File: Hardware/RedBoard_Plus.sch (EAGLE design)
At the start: 80 parts, among them IC3 LM1117, J2 ISP, J3 5.5x2.1mm Barrel, J4 QWIIC_RIGHT_ANGLE, J5 USB Female Type C Connector, Q1 20V/4.2A/52mΩ/1.4W, Q2 310mA/60V/1.6Ω, Q3 310mA/60V/1.6Ω, U3 3.3V, U4 ATMEGA328P_TQFP, U5 CH340C, Y1 16MHz

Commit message: Pete's design review notes:
SF logo on back
GND vias next to USB C
Remove 4-way nodes on sch
Remove overlapping text on sch
Move SFE logo in sch
Sch typo
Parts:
- removed U$78: REDBOARD_LOGO, redboard_logo:REDBOARD_LOGO
- added U$3: REDBOARD_LOGO, redboard_logo:REDBOARD_LOGO
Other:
- note added: "This switch is limited to 1.2A."
- note removed: "This switch is limited to 1.2VA."
- moved on the sheet: C8
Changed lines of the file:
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@@
 <attribute name="PROD_ID" value="DIO-09911"/>
 </part>
-<part name="SUPPLY7" library="SparkFun-PowerSymbols" deviceset="VIN" device=""/>
 <part name="D1" library="SparkFun-DiscreteSemi" deviceset="DIODE-SCHOTTKY" device="-SS14" value="1A/40V/500mV"/>
 <part name="JP11" library="SparkFun-Connectors" deviceset="M08" device="SMD-COMBO" value="JP11">
@@
 <part name="GND9" library="SparkFun-PowerSymbols" deviceset="GND" device=""/>
 <part name="J1" library="SparkFun-Connectors" deviceset="CONN_02" device="1X02_NO_SILK"/>
-<part name="U$78" library="redboard_logo" deviceset="REDBOARD_LOGO" device=""/>
-<part name="U$1" library="redboard_logo" deviceset="REDBOARD_LOGO" device=""/>
 <part name="FD1" library="SparkFun-Aesthetics" deviceset="FIDUCIAL" device="1X2"/>
 <part name="FD2" library="SparkFun-Aesthetics" deviceset="FIDUCIAL" device="1X2"/>
+<part name="U$1" library="redboard_logo" deviceset="REDBOARD_LOGO" device=""/>
+<part name="U$3" library="redboard_logo" deviceset="REDBOARD_LOGO" device=""/>
+<part name="SUPPLY25" library="SparkFun-PowerSymbols" deviceset="VIN" device=""/>
 </parts>
 <sheets>
@@
 30.8 mil width
 https://www.eeweb.com/tools/external-pcb-trace-max-current</text>
-<text x="220.98" y="144.78" size="1.778" layer="97" font="vector">This switch is limited to 1.2VA.</text>
+<text x="220.98" y="144.78" size="1.778" layer="97" font="vector">This switch is limited to 1.2A.</text>
 <wire x1="215.9" y1="279.4" x2="215.9" y2="81.28" width="0.2032" layer="97" style="longdash"/>
 <text x="183.642" y="264.16" size="2.54" layer="97" font="vector" align="center">PTH Connections</text>
@@
 <attribute name="VALUE" x="264.16" y="195.834" size="1.778" layer="96" align="bottom-center"/>
 </instance>
-<instance part="C8" gate="G$1" x="38.1" y="218.44" smashed="yes" rot="R90">
-<attribute name="NAME" x="35.179" y="219.964" size="1.778" layer="95" font="vector" rot="R90"/>
-<attribute name="VALUE" x="40.259" y="219.964" size="1.778" layer="96" font="vector" rot="R90"/>
+<instance part="C8" gate="G$1" x="35.56" y="218.44" smashed="yes" rot="R90">
+<attribute name="NAME" x="32.639" y="219.964" size="1.778" layer="95" font="vector" rot="R90"/>
+<attribute name="VALUE" x="37.719" y="219.964" size="1.778" layer="96" font="vector" rot="R90"/>
 </instance>
 <instance part="C10" gate="G$1" x="45.72" y="17.78" smashed="yes" rot="MR0">
@@
 <attribute name="VALUE" x="60.452" y="194.31" size="1.778" layer="96" font="vector"/>
 </instance>
-<instance part="JP1" gate="G$1" x="55.88" y="231.14" smashed="yes"/>
-<instance part="JP7" gate="G$1" x="83.566" y="242.062" smashed="yes"/>
+<instance part="JP1" gate="G$1" x="243.84" y="2.54" smashed="yes"/>
+<instance part="JP7" gate="G$1" x="233.426" y="5.842" smashed="yes"/>
 <instance part="J2" gate="G$1" x="27.94" y="157.48" smashed="yes">
 <attribute name="NAME" x="22.86" y="163.068" size="1.778" layer="95" font="vector"/>
@@
 <attribute name="VALUE" x="91.948" y="150.495" size="1.778" layer="96" font="vector" align="top-left"/>
 </instance>
-<instance part="SUPPLY7" gate="G$1" x="261.62" y="243.84" smashed="yes">
-<attribute name="VALUE" x="261.62" y="246.634" size="1.778" layer="96" align="bottom-center"/>
-</instance>
 <instance part="D1" gate="G$1" x="243.84" y="241.3" smashed="yes">
 <attribute name="NAME" x="246.38" y="241.7826" size="1.778" layer="95"/>
@@
 <instance part="BYP" gate="G$1" x="53.34" y="45.72" smashed="yes">
 <attribute name="NAME" x="51.054" y="47.752" size="1.778" layer="95" font="vector"/>
-<attribute name="VALUE" x="50.8" y="43.18" size="1.778" layer="96" font="vector" align="top-left"/>
 </instance>
 <instance part="F2" gate="F1" x="53.34" y="33.02" smashed="yes">
@@
 <attribute name="NAME" x="172.72" y="205.232" size="1.778" layer="95" font="vector" rot="R180"/>
 </instance>
-<instance part="U$78" gate="G$1" x="403.86" y="40.64" smashed="yes"/>
-<instance part="U$1" gate="G$1" x="375.92" y="40.64" smashed="yes"/>
 <instance part="FD1" gate="G$1" x="424.18" y="17.78" smashed="yes"/>
 <instance part="FD2" gate="G$1" x="426.72" y="17.78" smashed="yes"/>
+<instance part="U$1" gate="G$1" x="403.86" y="40.64" smashed="yes"/>
+<instance part="U$3" gate="G$1" x="378.46" y="40.64" smashed="yes"/>
+<instance part="SUPPLY25" gate="G$1" x="259.08" y="243.84" smashed="yes">
+<attribute name="VALUE" x="259.08" y="246.634" size="1.778" layer="96" align="bottom-center"/>
+</instance>
 </instances>
 <busses>
@@
 <pinref part="C5" gate="G$1" pin="+"/>
 <pinref part="IC3" gate="G$1" pin="IN"/>
-<wire x1="261.62" y1="241.3" x2="246.38" y2="241.3" width="0.1524" layer="91"/>
-<pinref part="SUPPLY7" gate="G$1" pin="VIN"/>
+<wire x1="261.62" y1="241.3" x2="259.08" y2="241.3" width="0.1524" layer="91"/>
 <pinref part="D1" gate="G$1" pin="C"/>
-<wire x1="261.62" y1="243.84" x2="261.62" y2="241.3" width="0.1524" layer="91"/>
+<wire x1="259.08" y1="241.3" x2="246.38" y2="241.3" width="0.1524" layer="91"/>
+<wire x1="259.08" y1="241.3" x2="259.08" y2="243.84" width="0.1524" layer="91"/>
+<junction x="259.08" y="241.3"/>
+<pinref part="SUPPLY25" gate="G$1" pin="VIN"/>
 </segment>
 <segment>
@@
 <pinref part="C15" gate="G$1" pin="+"/>
 <wire x1="60.96" y1="33.02" x2="63.5" y2="33.02" width="0.1524" layer="91"/>
-<wire x1="63.5" y1="33.02" x2="68.58" y2="33.02" width="0.1524" layer="91"/>
+<wire x1="63.5" y1="33.02" x2="66.04" y2="33.02" width="0.1524" layer="91"/>
+<wire x1="66.04" y1="33.02" x2="68.58" y2="33.02" width="0.1524" layer="91"/>
 <wire x1="68.58" y1="22.86" x2="68.58" y2="33.02" width="0.1524" layer="91"/>
 <pinref part="C12" gate="G$1" pin="1"/>
@@
 <junction x="68.58" y="33.02"/>
 <pinref part="BYP" gate="G$1" pin="2"/>
-<wire x1="58.42" y1="45.72" x2="63.5" y2="45.72" width="0.1524" layer="91"/>
-<wire x1="63.5" y1="45.72" x2="63.5" y2="33.02" width="0.1524" layer="91"/>
+<wire x1="58.42" y1="45.72" x2="66.04" y2="45.72" width="0.1524" layer="91"/>
 <pinref part="F2" gate="F1" pin="2"/>
+<wire x1="66.04" y1="45.72" x2="66.04" y2="33.02" width="0.1524" layer="91"/>
+<junction x="66.04" y="33.02"/>
 </segment>
 </net>
@@
 <junction x="45.72" y="33.02"/>
 <pinref part="JP14" gate="JP1" pin="1"/>
-<wire x1="35.56" y1="33.02" x2="45.72" y2="33.02" width="0.1524" layer="91"/>
+<wire x1="35.56" y1="33.02" x2="43.18" y2="33.02" width="0.1524" layer="91"/>
+<wire x1="43.18" y1="33.02" x2="45.72" y2="33.02" width="0.1524" layer="91"/>
 <wire x1="25.4" y1="50.8" x2="35.56" y2="50.8" width="0.1524" layer="91"/>
 <wire x1="35.56" y1="50.8" x2="35.56" y2="33.02" width="0.1524" layer="91"/>
 <junction x="35.56" y="33.02"/>
 <pinref part="BYP" gate="G$1" pin="1"/>
-<wire x1="48.26" y1="45.72" x2="45.72" y2="45.72" width="0.1524" layer="91"/>
-<wire x1="45.72" y1="45.72" x2="45.72" y2="33.02" width="0.1524" layer="91"/>
 <pinref part="F2" gate="F1" pin="1"/>
+<wire x1="48.26" y1="45.72" x2="43.18" y2="45.72" width="0.1524" layer="91"/>
+<wire x1="43.18" y1="45.72" x2="43.18" y2="33.02" width="0.1524" layer="91"/>
+<junction x="43.18" y="33.02"/>
 </segment>
 </net>
@@
 <net name="!DTR" class="0">
 <segment>
-<wire x1="33.02" y1="218.44" x2="30.48" y2="218.44" width="0.1524" layer="91"/>
+<wire x1="30.48" y1="218.44" x2="27.94" y2="218.44" width="0.1524" layer="91"/>
 <pinref part="C8" gate="G$1" pin="1"/>
-<label x="30.48" y="218.44" size="1.27" layer="95" font="vector" rot="R180" xref="yes"/>
+<label x="27.94" y="218.44" size="1.27" layer="95" font="vector" rot="R180" xref="yes"/>
 </segment>
 <segment>
@@
 <pinref part="R3" gate="G$1" pin="1"/>
 <pinref part="C8" gate="G$1" pin="2"/>
+<wire x1="38.1" y1="218.44" x2="40.64" y2="218.44" width="0.1524" layer="91"/>
 <wire x1="40.64" y1="218.44" x2="43.18" y2="218.44" width="0.1524" layer="91"/>
-<label x="43.18" y="220.98" size="1.27" layer="95" font="vector" rot="R90" xref="yes"/>
-<wire x1="43.18" y1="220.98" x2="43.18" y2="218.44" width="0.1524" layer="91"/>
 <pinref part="U4" gate="U1" pin="PC6(/RESET)"/>
 <pinref part="S1" gate="G$1" pin="2"/>
-</segment>
-<segment>
+<wire x1="40.64" y1="218.44" x2="40.64" y2="220.98" width="0.1524" layer="91"/>
+<junction x="40.64" y="218.44"/>
+<label x="40.64" y="220.98" size="1.27" layer="95" rot="R90" xref="yes"/>
+</segment>
+<segment>

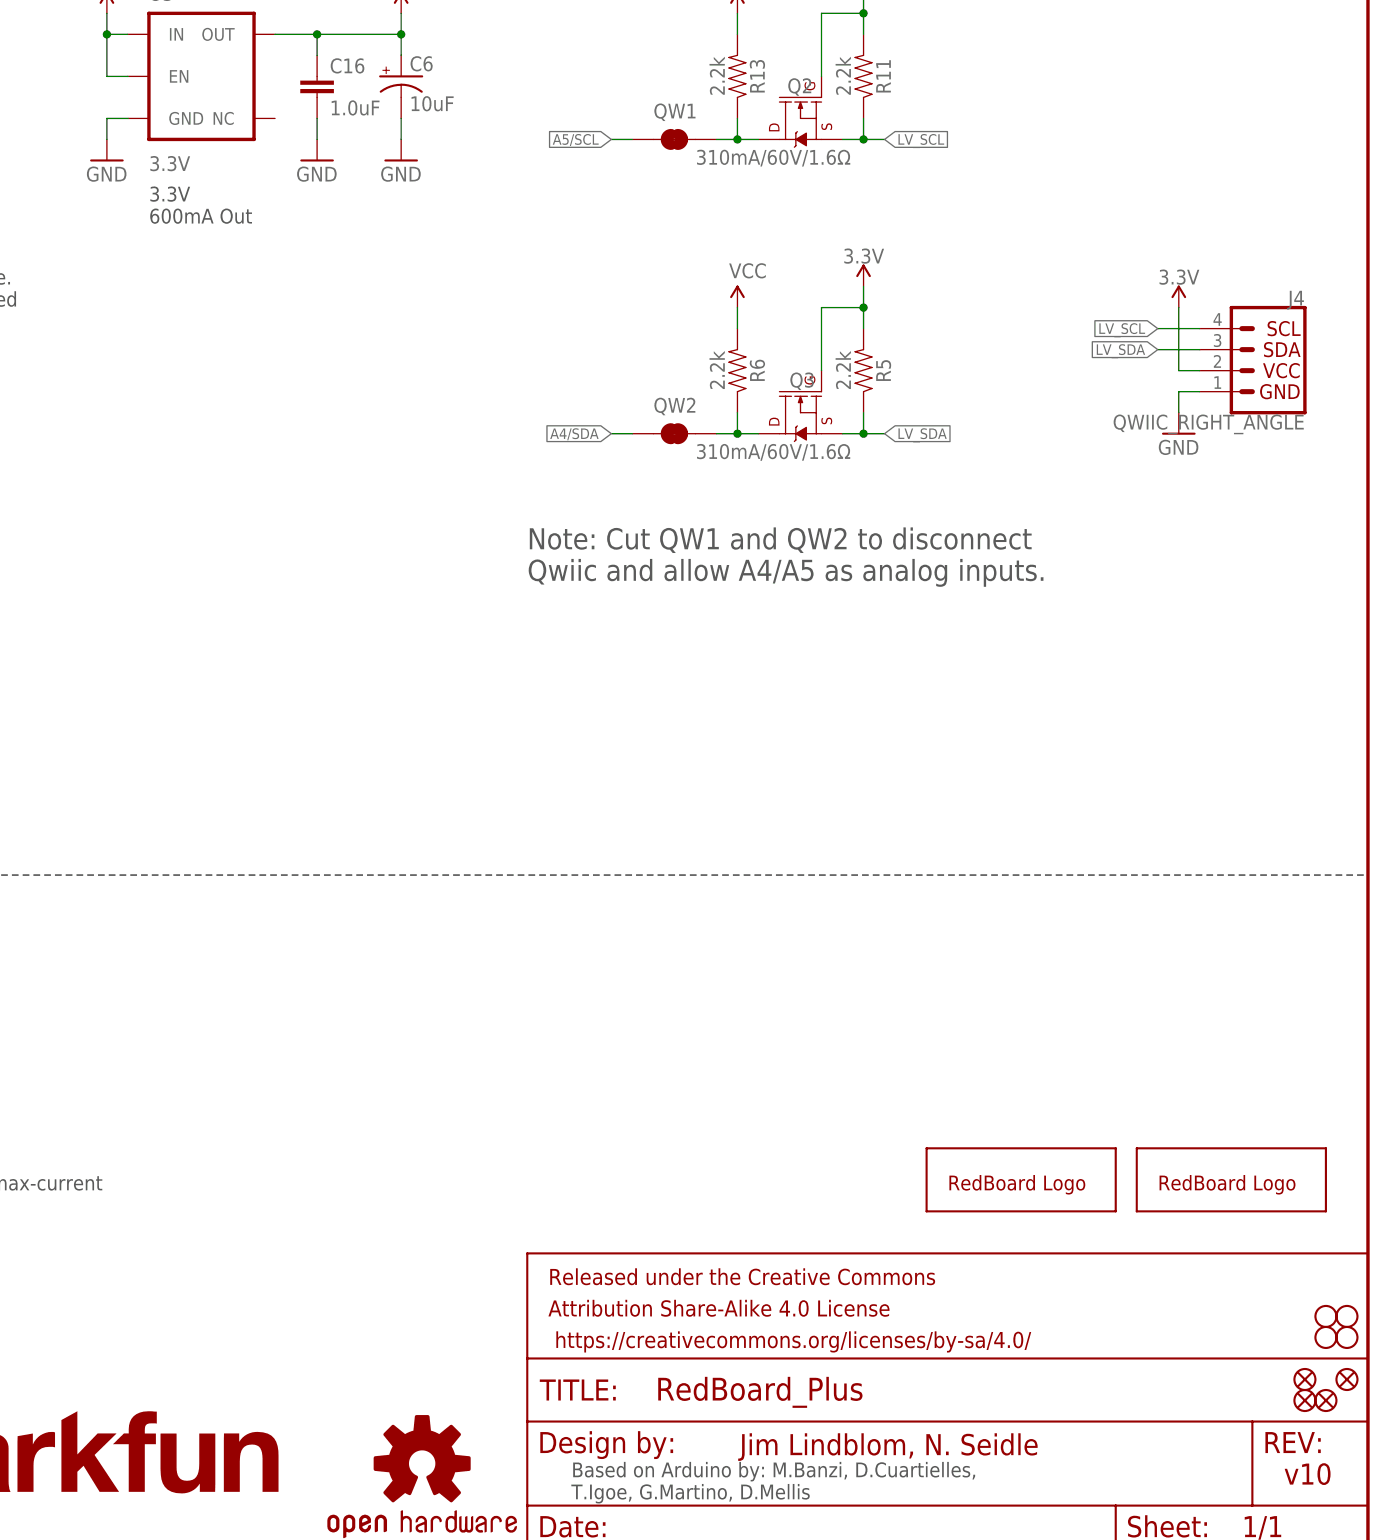
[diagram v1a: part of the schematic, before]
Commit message: Design review changes
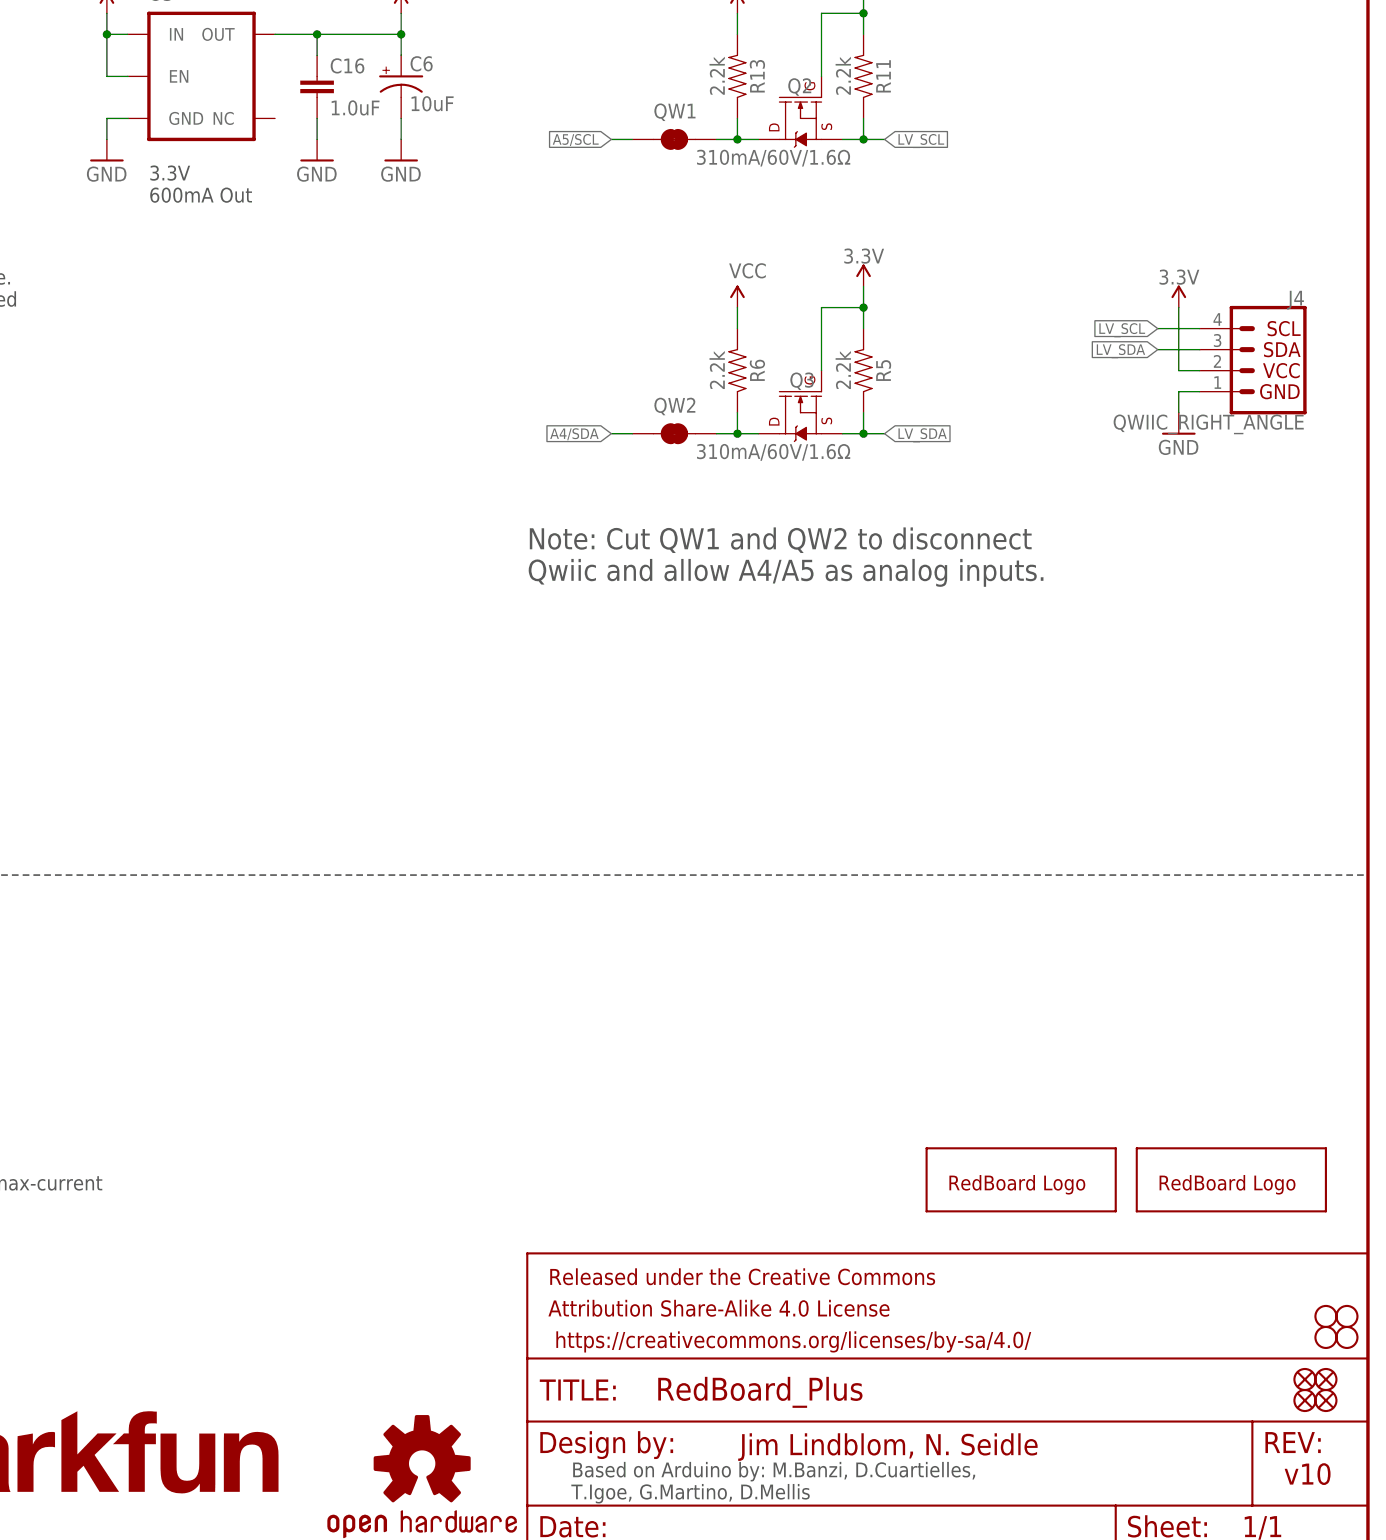
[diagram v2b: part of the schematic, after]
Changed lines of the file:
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@@
 <text x="421.64" y="7.62" size="2.54" layer="94" font="vector">v10</text>
 <text x="225.044" y="245.872" size="1.778" layer="97" font="vector">VIN Range: 7-15V</text>
-<text x="284.48" y="160.02" size="1.778" layer="97" font="vector">3.3V
+<text x="284.48" y="162.56" size="1.778" layer="97" font="vector">3.3V
 600mA Out</text>
 <text x="229.616" y="157.48" size="2.54" layer="97" font="vector">Board I/O Voltage</text>
@@
 <instance part="JP6" gate="G$1" x="429.26" y="25.4" smashed="yes"/>
 <instance part="JP8" gate="G$1" x="424.18" y="20.32" smashed="yes"/>
-<instance part="JP9" gate="G$1" x="429.26" y="20.32" smashed="yes"/>
+<instance part="JP9" gate="G$1" x="426.72" y="20.32" smashed="yes"/>
 <instance part="U$16" gate="G$1" x="317.5" y="10.16" smashed="yes"/>
 <instance part="C12" gate="G$1" x="63.5" y="17.78" smashed="yes" rot="MR0">
@@
 <instance part="U3" gate="G$1" x="292.1" y="177.8" smashed="yes">
 <attribute name="NAME" x="284.48" y="186.944" size="1.778" layer="95"/>
-<attribute name="VALUE" x="284.48" y="166.37" size="1.778" layer="96"/>
 </instance>
 <instance part="C16" gate="G$1" x="304.8" y="175.26" smashed="yes">
